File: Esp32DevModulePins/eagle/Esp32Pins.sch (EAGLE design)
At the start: 2 parts

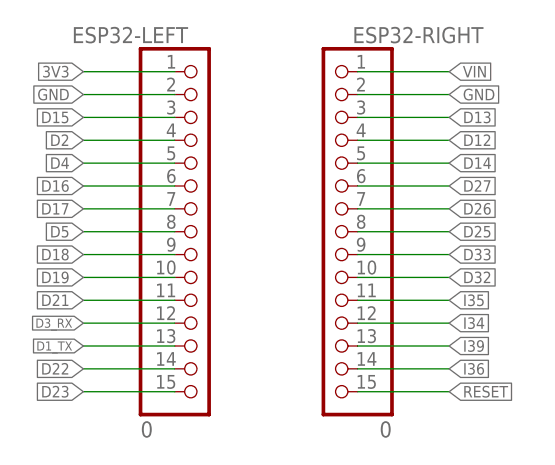
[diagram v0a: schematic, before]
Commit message: Corrected left vs right nomenclature
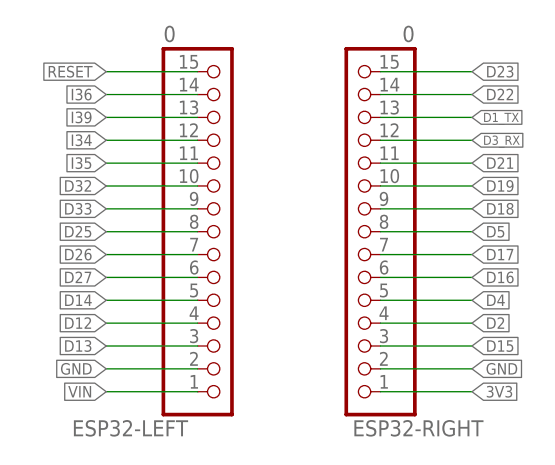
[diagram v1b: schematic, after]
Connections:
- net 3V3: now also ESP32-RIGHT.1; no longer ESP32-LEFT.1
- net D12: now also ESP32-LEFT.4; no longer ESP32-RIGHT.4
- net D13: now also ESP32-LEFT.3; no longer ESP32-RIGHT.3
- net D14: now also ESP32-LEFT.5; no longer ESP32-RIGHT.5
- net D15: now also ESP32-RIGHT.3; no longer ESP32-LEFT.3
- net D16: now also ESP32-RIGHT.6; no longer ESP32-LEFT.6
- net D17: now also ESP32-RIGHT.7; no longer ESP32-LEFT.7
- net D18: now also ESP32-RIGHT.9; no longer ESP32-LEFT.9
- net D19: now also ESP32-RIGHT.10; no longer ESP32-LEFT.10
- net D1_TX: now also ESP32-RIGHT.13; no longer ESP32-LEFT.13
- net D2: now also ESP32-RIGHT.4; no longer ESP32-LEFT.4
- net D21: now also ESP32-RIGHT.11; no longer ESP32-LEFT.11
- net D22: now also ESP32-RIGHT.14; no longer ESP32-LEFT.14
- net D23: now also ESP32-RIGHT.15; no longer ESP32-LEFT.15
- net D25: now also ESP32-LEFT.8; no longer ESP32-RIGHT.8
- net D26: now also ESP32-LEFT.7; no longer ESP32-RIGHT.7
- net D27: now also ESP32-LEFT.6; no longer ESP32-RIGHT.6
- net D32: now also ESP32-LEFT.10; no longer ESP32-RIGHT.10
- net D33: now also ESP32-LEFT.9; no longer ESP32-RIGHT.9
- net D3_RX: now also ESP32-RIGHT.12; no longer ESP32-LEFT.12
- net D4: now also ESP32-RIGHT.5; no longer ESP32-LEFT.5
- net D5: now also ESP32-RIGHT.8; no longer ESP32-LEFT.8
- net I34: now also ESP32-LEFT.12; no longer ESP32-RIGHT.12
- net I35: now also ESP32-LEFT.11; no longer ESP32-RIGHT.11
- net I36: now also ESP32-LEFT.14; no longer ESP32-RIGHT.14
- net I39: now also ESP32-LEFT.13; no longer ESP32-RIGHT.13
- net RESET: now also ESP32-LEFT.15; no longer ESP32-RIGHT.15
- net VIN: now also ESP32-LEFT.1; no longer ESP32-RIGHT.1
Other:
- moved on the sheet: ESP32-LEFT, ESP32-RIGHT
